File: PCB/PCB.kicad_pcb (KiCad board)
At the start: 2 copper layers, 25.4 x 25.4 mm, 26 parts, among them J1 , J2 , J3 PROG, SW1 ADDR, U1 ATtiny806-M

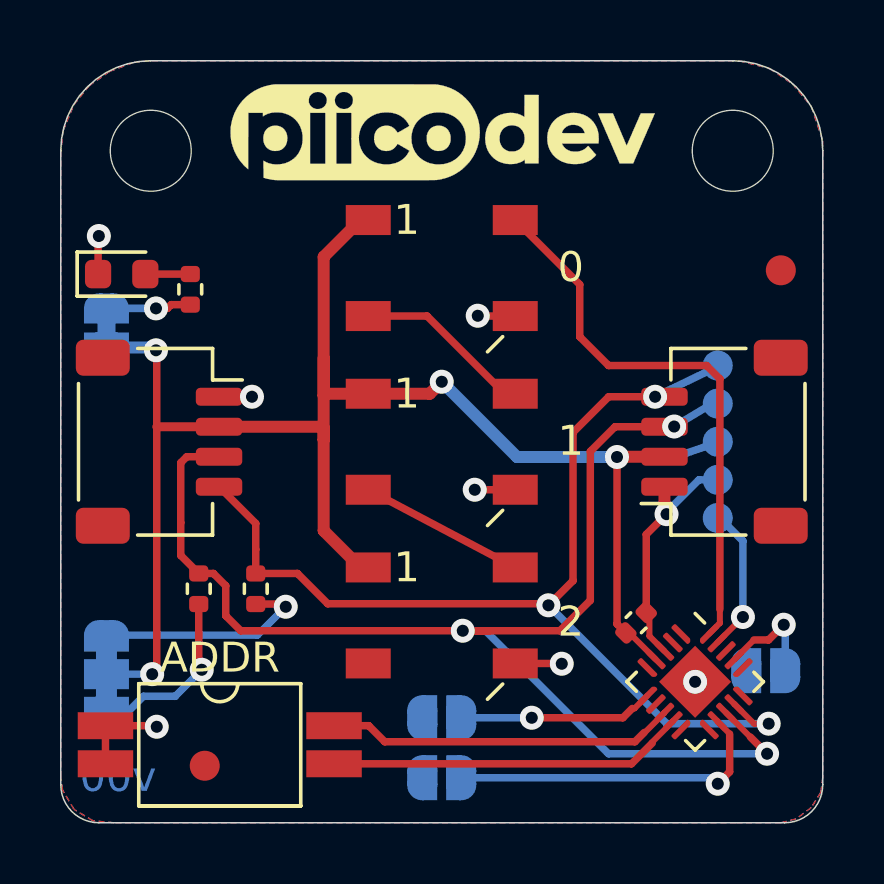
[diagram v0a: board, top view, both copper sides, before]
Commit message: Make pwr LED user controllable
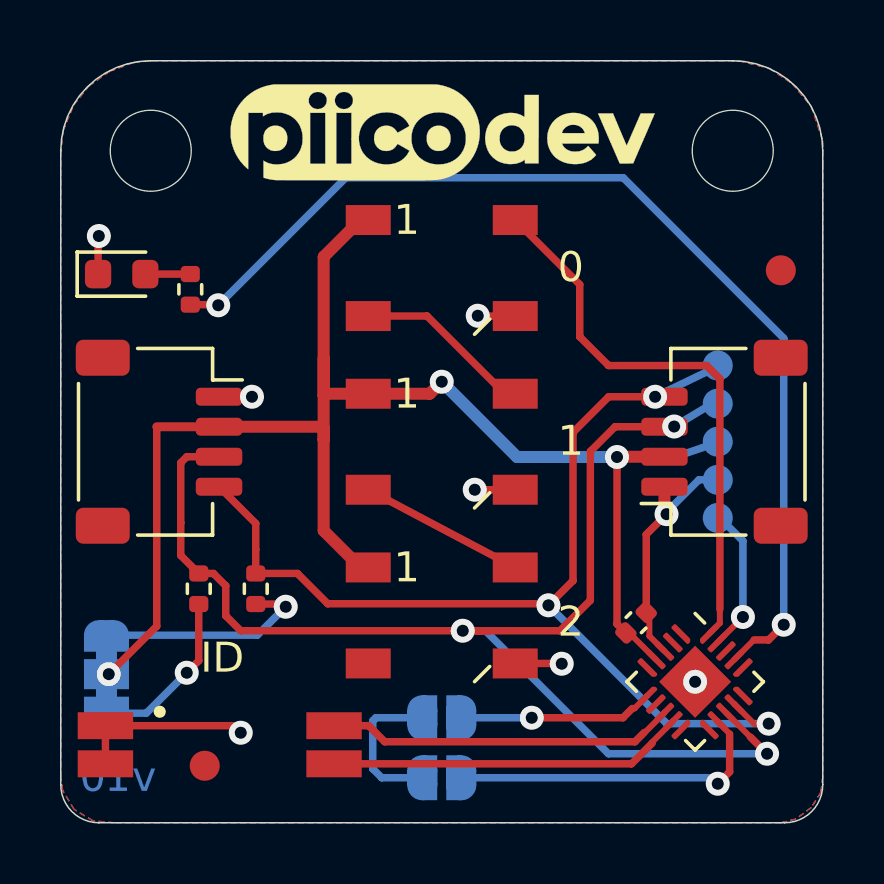
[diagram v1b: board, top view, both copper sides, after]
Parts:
- removed JP1: LED, CoreElectronics_Components:SolderJumper-2_P1.3mm_Bridged_RoundedPad1.0x1.5mm
- removed JP4: FACTORY RESET, Jumper:SolderJumper-2_P1.3mm_Open_RoundedPad1.0x1.5mm
- J3: footprint CoreElectronics_Components:PiicoDev_ProgrammingHeader_2x03_P1.27mm_Vertical -> CoreElectronics_Components:PiicoDev_header_programming_test_1x05_P1.27mm_Vertical
- JP3: value ADD2 -> ADD3
- JP5: value ADD3 -> ADD4
- R1: value 1k -> 4k7
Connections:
- JP3 pad 1: /ADD4 -> /ADD3
- JP5 pad 1: /ADD3 -> /ADD4
- R1 pad 1: Net-(JP1-Pad2) -> /PWR_LED
- SW1 pad 3: /ADD1 -> /ADD2
- SW1 pad 4: /ADD2 -> /ADD1
- U1 pad 12: /ADD3 -> /ADD4
- U1 pad 17: /FAC_RST -> /PWR_LED
- U1 pad 6: /ADD4 -> /ADD3
- U1 pad 8: /ADD2 -> /ADD1
- U1 pad 9: /ADD1 -> /ADD2
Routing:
- net /PWR_LED: track 0.00 -> 35.5 mm, vias 0 -> 2
- net GND: track 17.9 -> 25.8 mm
- net +3V3: track 57.9 -> 52.8 mm, vias 4 -> 3
- net /ADD4: track 6.51 -> 11.1 mm
- net /ADD3: track 11.1 -> 6.51 mm
- net /FAC_RST: track 3.68 -> 0.00 mm, vias 1 -> 0
- net Net-(JP1-Pad2): track 2.85 -> 0.00 mm, vias 1 -> 0
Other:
- board text added: "ID"
- board text added: "v10"
- board text removed: "ADDR"
- board text removed: "PWR LED"
- board text removed: "RST"
- board text removed: "v00"

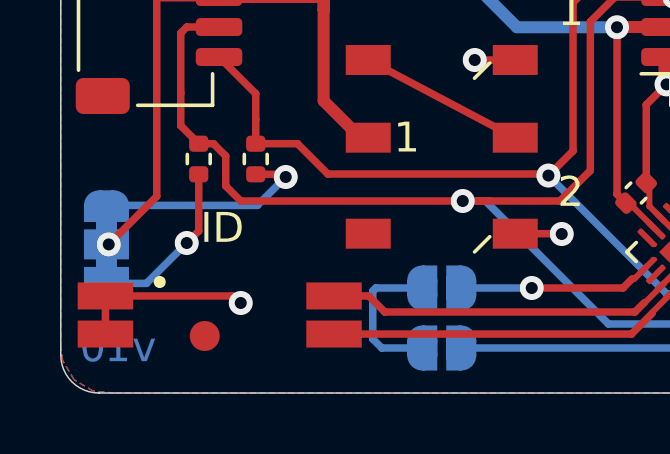
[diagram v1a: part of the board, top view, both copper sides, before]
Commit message: rotate ID switch
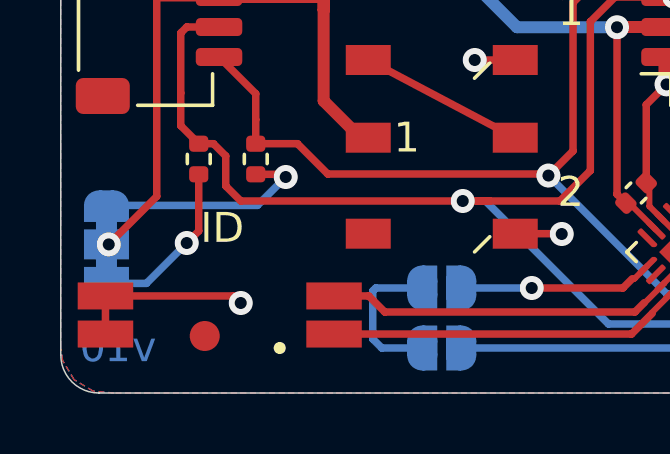
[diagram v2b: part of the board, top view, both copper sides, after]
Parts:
- turned SW1 to 180 degrees
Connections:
- D4 pad 2: (no net) -> Net-(D4-Pad2)
- SW1 pad 1: GND -> /ADD2
- SW1 pad 2: GND -> /ADD1
- SW1 pad 3: /ADD2 -> GND
- SW1 pad 4: /ADD1 -> GND
- U1 pad 1: (no net) -> Net-(U1-Pad1)
- U1 pad 10: (no net) -> Net-(U1-Pad10)
- U1 pad 11: (no net) -> Net-(U1-Pad11)
- U1 pad 15: (no net) -> Net-(U1-Pad15)
- U1 pad 16: (no net) -> Net-(U1-Pad16)
- U1 pad 18: (no net) -> Net-(U1-Pad18)
- U1 pad 2: (no net) -> Net-(U1-Pad2)
- U1 pad 5: (no net) -> Net-(U1-Pad5)
- U1 pad 7: (no net) -> Net-(U1-Pad7)
